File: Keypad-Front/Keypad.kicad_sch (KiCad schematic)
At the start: 99 parts, among them J1 RTC STEMMA QT, J6 EXP QWIIC, J7 TOUCH QWIIC, U1 DS3231MZ, U2 PCA9536DP, U3 CAP1214, U4 PN5321A3HN_C1xx, U5 MCP9808_MSOP, Y3 27.12MHz

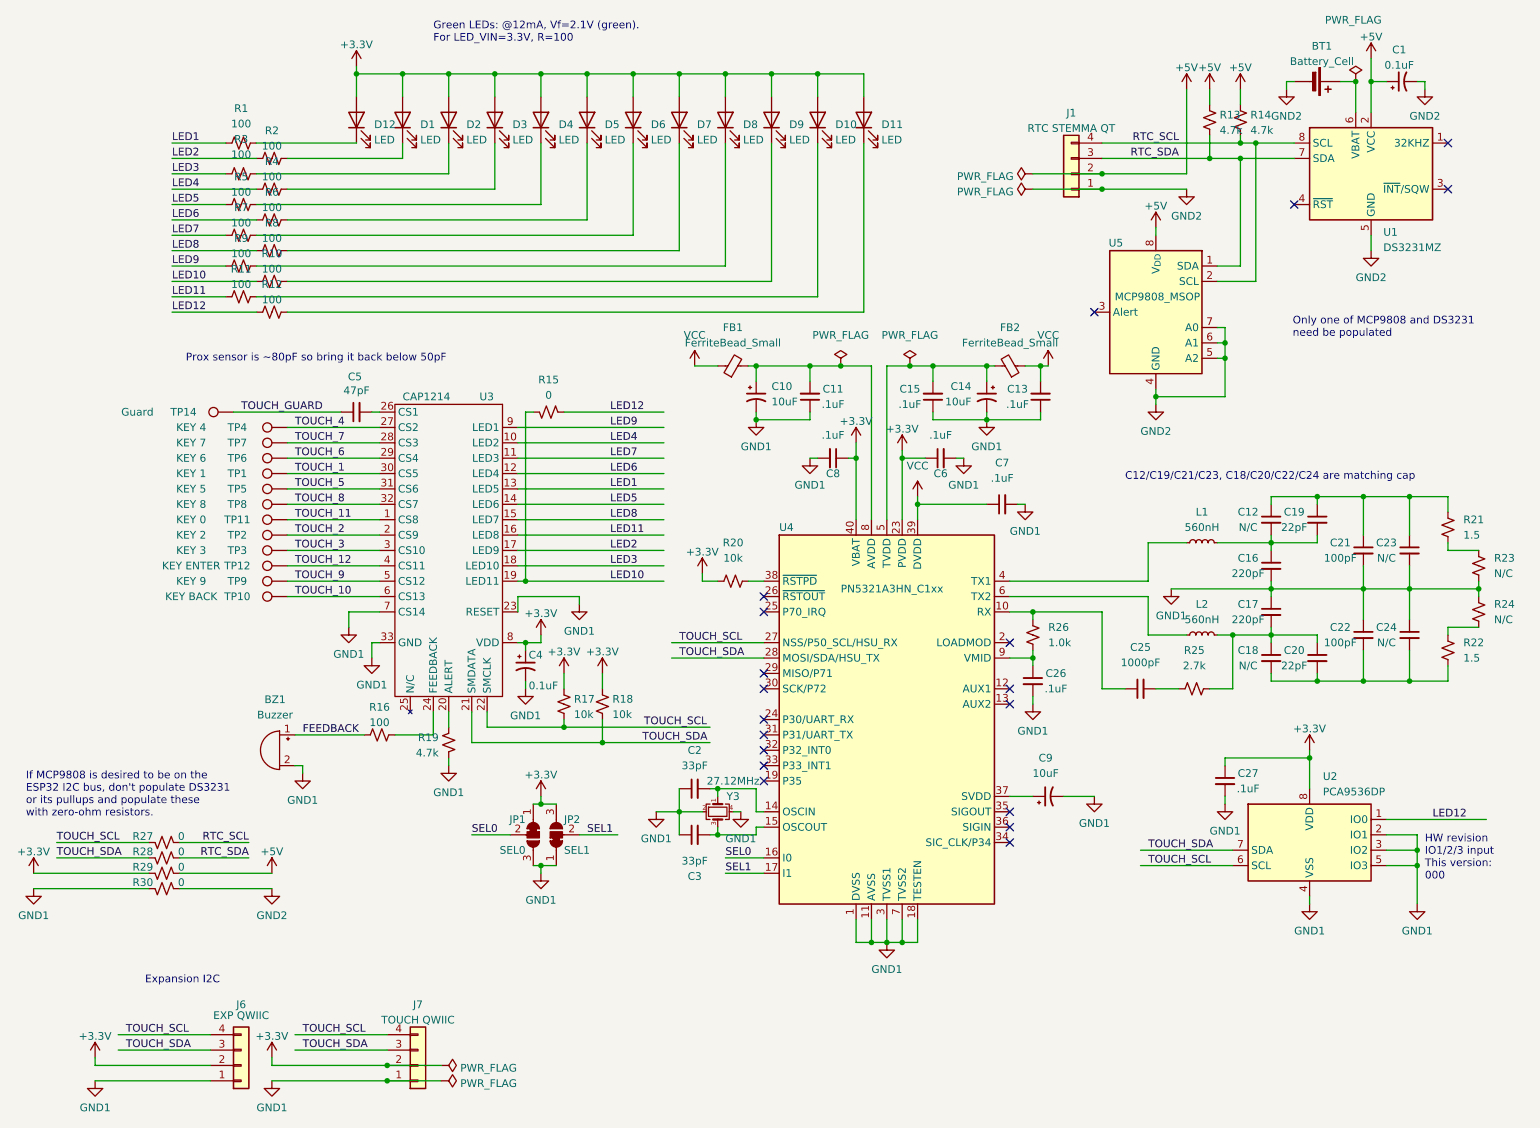
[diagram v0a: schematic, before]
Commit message: Simplify schematic and PCB
Remove the solder jumper for SEL0/SEL1, that's been tested & is correct.

Add 0-ohm resistors for GPIO expander to accomodate future green wire hacks.

Mark the DNP components on the schematic.
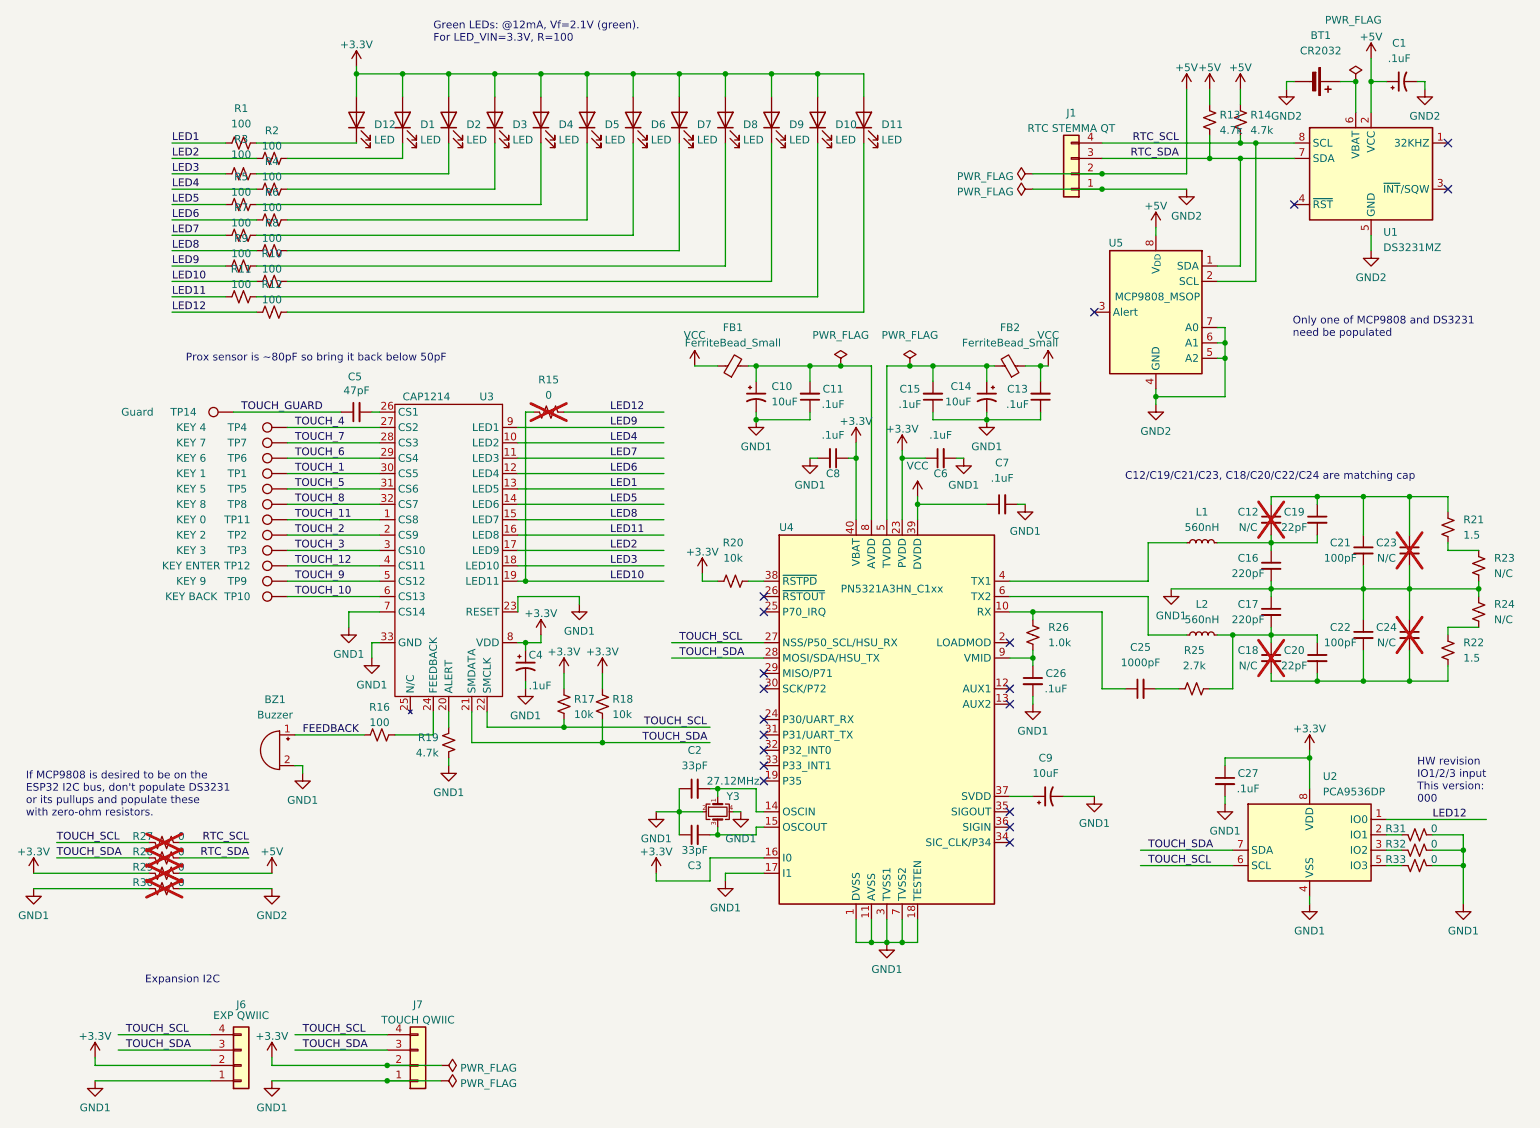
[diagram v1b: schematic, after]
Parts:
- removed JP1: SEL0, Jumper:SolderJumper-3_P1.3mm_Bridged12_Pad1.0x1.5mm, symbol Jumper:SolderJumper_3_Bridged12
- removed JP2: SEL1, Jumper:SolderJumper-3_P1.3mm_Bridged12_Pad1.0x1.5mm, symbol Jumper:SolderJumper_3_Bridged12
- added R31, R32, R33: 0, Resistor_SMD:R_0805_2012Metric_Pad1.20x1.40mm_HandSolder, symbol Device:R_Small_US
- BT1: value Battery_Cell -> CR2032
- C1, C4: value 0.1uF -> .1uF
- C12, C18, C23, C24, R15, R27, R28, R29, R30: now not fitted
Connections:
- net SEL0 is gone; now on net +3.3V: U4.16 (I0)
- net SEL1 is gone; now on net GND1: U4.17 (I1)
- net GND1: now also R31.2, R32.2, R33.2; no longer U2.2 (IO1), U2.3 (IO2), U2.5 (IO3)
- new net: R33.1, U2.5 (IO3)
- new net: R31.1, U2.2 (IO1)
- new net: R32.1, U2.3 (IO2)

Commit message: More schematic cleanup
* Remove silkscreen for R23/R24, which are shorted jumpers as a netlist
hack for the PCB antenna, not "real" components.

* Remove unnecessary R15 (and its traces) now that we have PCA9536 to
drive LED12.
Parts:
- removed R15: 0, Resistor_SMD:R_0805_2012Metric_Pad1.20x1.40mm_HandSolder, symbol Device:R_Small_US
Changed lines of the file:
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@@
   (junction (at 80.01 191.77) (diameter 0) (color 0 0 0 0)
-  )
-  (junction (at 102.87 109.22) (diameter 0) (color 0 0 0 0)
   )
   (junction (at 198.12 44.45) (diameter 0) (color 0 0 0 0)
@@
     (stroke (width 0) (type default))
   )
-  (wire (pts (xy 109.22 81.28) (xy 125.73 81.28))
-    (stroke (width 0) (type default))
-  )
   (wire (pts (xy 242.57 26.67) (xy 245.11 26.67))
     (stroke (width 0) (type default))
@@
     (stroke (width 0) (type default))
   )
-  (wire (pts (xy 102.87 81.28) (xy 102.87 109.22))
-    (stroke (width 0) (type default))
-  )
   (wire (pts (xy 45.72 160.02) (xy 60.96 160.02))
     (stroke (width 0) (type default))
@@
     (stroke (width 0) (type default))
   )
-  (wire (pts (xy 102.87 109.22) (xy 125.73 109.22))
+  (wire (pts (xy 101.6 109.22) (xy 125.73 109.22))
     (stroke (width 0) (type default))
   )
@@
     (stroke (width 0) (type default))
   )
-  (wire (pts (xy 101.6 109.22) (xy 102.87 109.22))
-    (stroke (width 0) (type default))
-  )
   (wire (pts (xy 220.98 57.15) (xy 220.98 39.37))
     (stroke (width 0) (type default))
@@
   )
   (wire (pts (xy 248.92 120.65) (xy 248.92 125.73))
-    (stroke (width 0) (type default))
-  )
-  (wire (pts (xy 104.14 81.28) (xy 102.87 81.28))
     (stroke (width 0) (type default))
   )
@@
   )
   (label "TOUCH_SCL" (at 66.04 184.15 0) (fields_autoplaced)
-    (effects (font (size 1.27 1.27)) (justify left bottom))
-  )
-  (label "LED12" (at 116.84 81.28 0) (fields_autoplaced)
     (effects (font (size 1.27 1.27)) (justify left bottom))
   )
@@
         )
       )
-    )
-  )
-  (symbol (lib_id "Device:R_Small_US") (at 106.68 81.28 90) (mirror x) (unit 1)
-    (in_bom yes) (on_board yes) (dnp yes) (fields_autoplaced)
-    (property "Reference" "R15" (at 106.68 75.946 90)
-      (effects (font (size 1.27 1.27)))
-    )
-    (property "Value" "0" (at 106.68 78.486 90)
-      (effects (font (size 1.27 1.27)))
-    )
-    (property "Footprint" "Resistor_SMD:R_0805_2012Metric_Pad1.20x1.40mm_HandSolder" (at 106.68 81.28 0)
-      (effects (font (size 1.27 1.27)) hide)
-    )
-    (property "Datasheet" "~" (at 106.68 81.28 0)
-      (effects (font (size 1.27 1.27)) hide)
-    )
-    (pin "1")
-    (pin "2")
-    (instances
-      (project "Keypad"
-        (path "/ed47ce54-8b56-4a78-a942-9443bc7041ac"
-          (reference "R15") (unit 1)
-        )
-      )
